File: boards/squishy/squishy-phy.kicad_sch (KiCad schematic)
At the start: 5 parts, among them Q2 Q_NMOS_GSD, U1 LFE5U-45F-8BG256

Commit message: hardware: cleaned up the schematics a bit and made them more unified
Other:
- company: (none) -> Shrine Maiden Heavy Industries
- title: (none) -> Squishy - Multitool - SCSI PHY
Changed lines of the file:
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@@
 (kicad_sch (version 20211123) (generator eeschema)
-  (paper "A4")
+  (paper "A3")
+  (title_block
+    (title "Squishy - Multitool - SCSI PHY")
+    (date "2021-12-21")
+    (rev "2")
+    (company "Shrine Maiden Heavy Industries")
+    (comment 1 "License:  CERN-OHL-S")
+    (comment 2 "© 2020 Aki 'lethalbit' Van Ness, et. al.")
+    (comment 3 "Multi-voltaga diff/se SCSI PHY for SCSI-1 2 and 3")
+    (comment 4 "Squishy - SCSI multitool and gateware library")
+  )
   (junction (at 199.39 59.69) (diameter 0) (color 0 0 0 0)
   )
@@
   (symbol (lib_id "power:GND") (at 199.39 74.93 0) (unit 1)
     (in_bom yes) (on_board yes)
-    (property "Reference" "#PWR?" (id 0) (at 199.39 81.28 0)
+    (property "Reference" "#PWR024" (id 0) (at 199.39 81.28 0)
       (effects (font (size 1.27 1.27)) hide)
     )
@@
   (symbol (lib_id "power:+3V3") (at 199.39 49.53 0) (unit 1)
     (in_bom yes) (on_board yes)
-    (property "Reference" "#PWR?" (id 0) (at 199.39 53.34 0)
+    (property "Reference" "#PWR023" (id 0) (at 199.39 53.34 0)
       (effects (font (size 1.27 1.27)) hide)
     )

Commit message: hardware: some ERC cleanup
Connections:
- no-connect marks 89 -> 88
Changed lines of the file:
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@@
   (no_connect (at 86.36 43.18))
   (no_connect (at 125.73 163.83))
-  (no_connect (at 123.19 78.74))
   (no_connect (at 121.92 55.88))
   (no_connect (at 85.09 80.01))

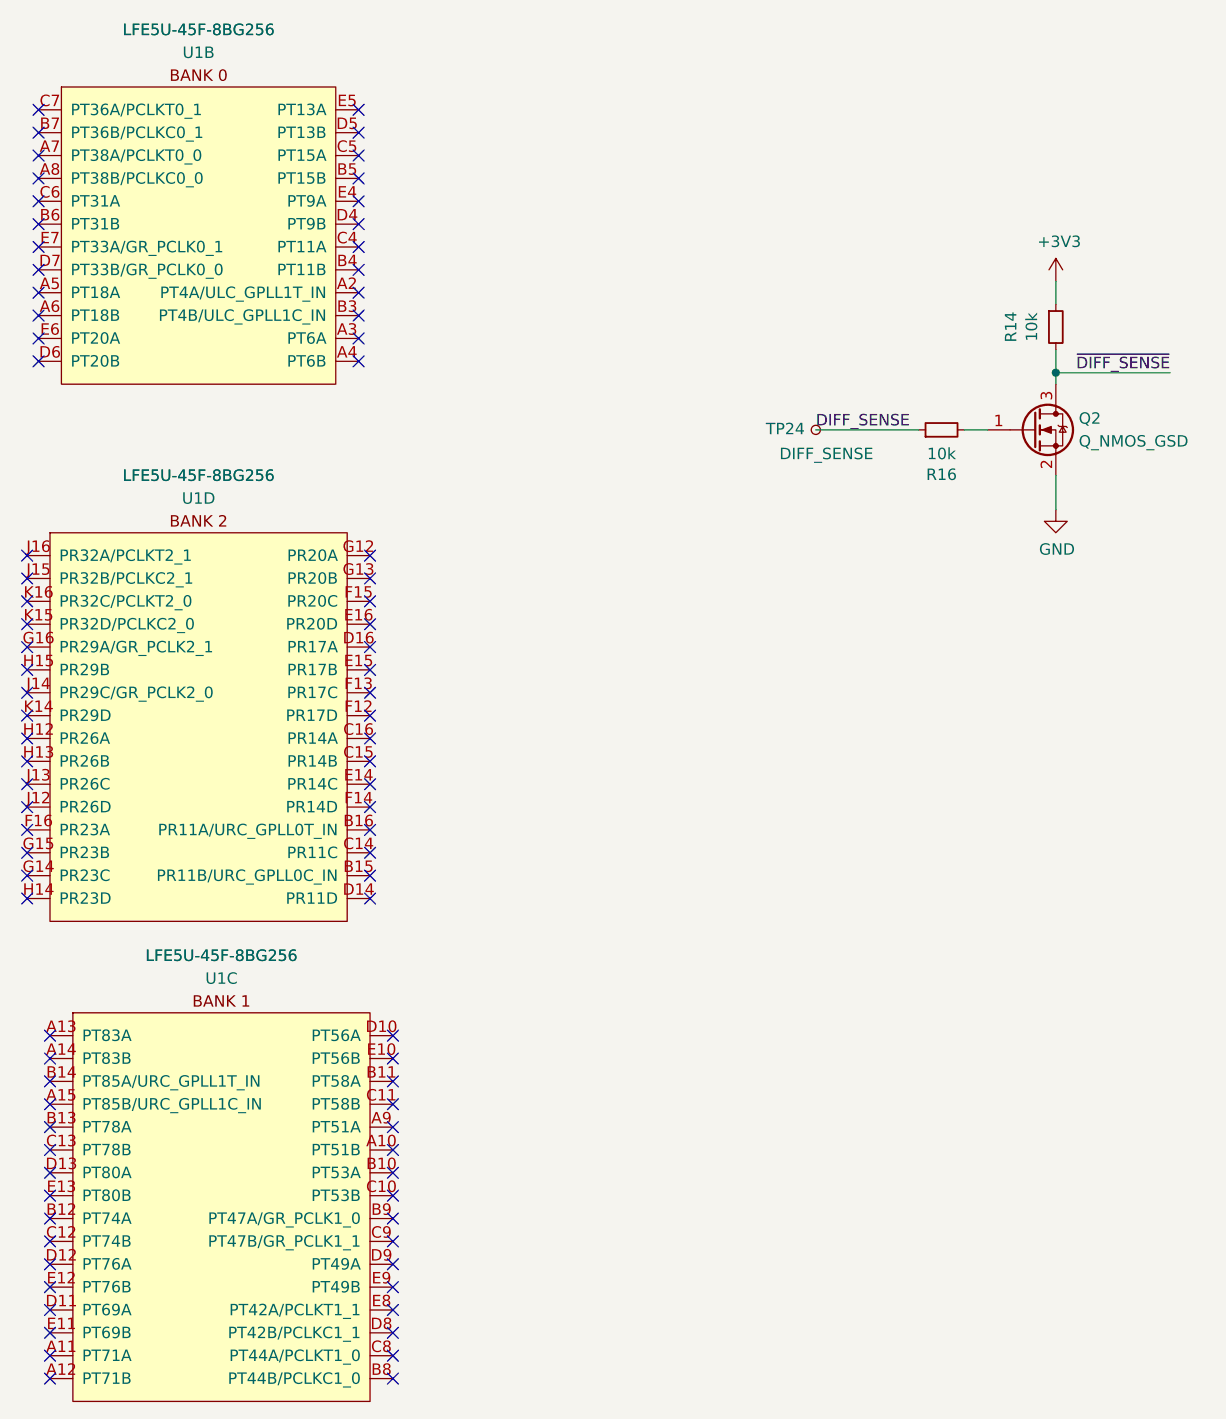
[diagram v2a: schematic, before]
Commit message: hardware: started gutting the old FPGA in preparation to migrate to the new FPGA
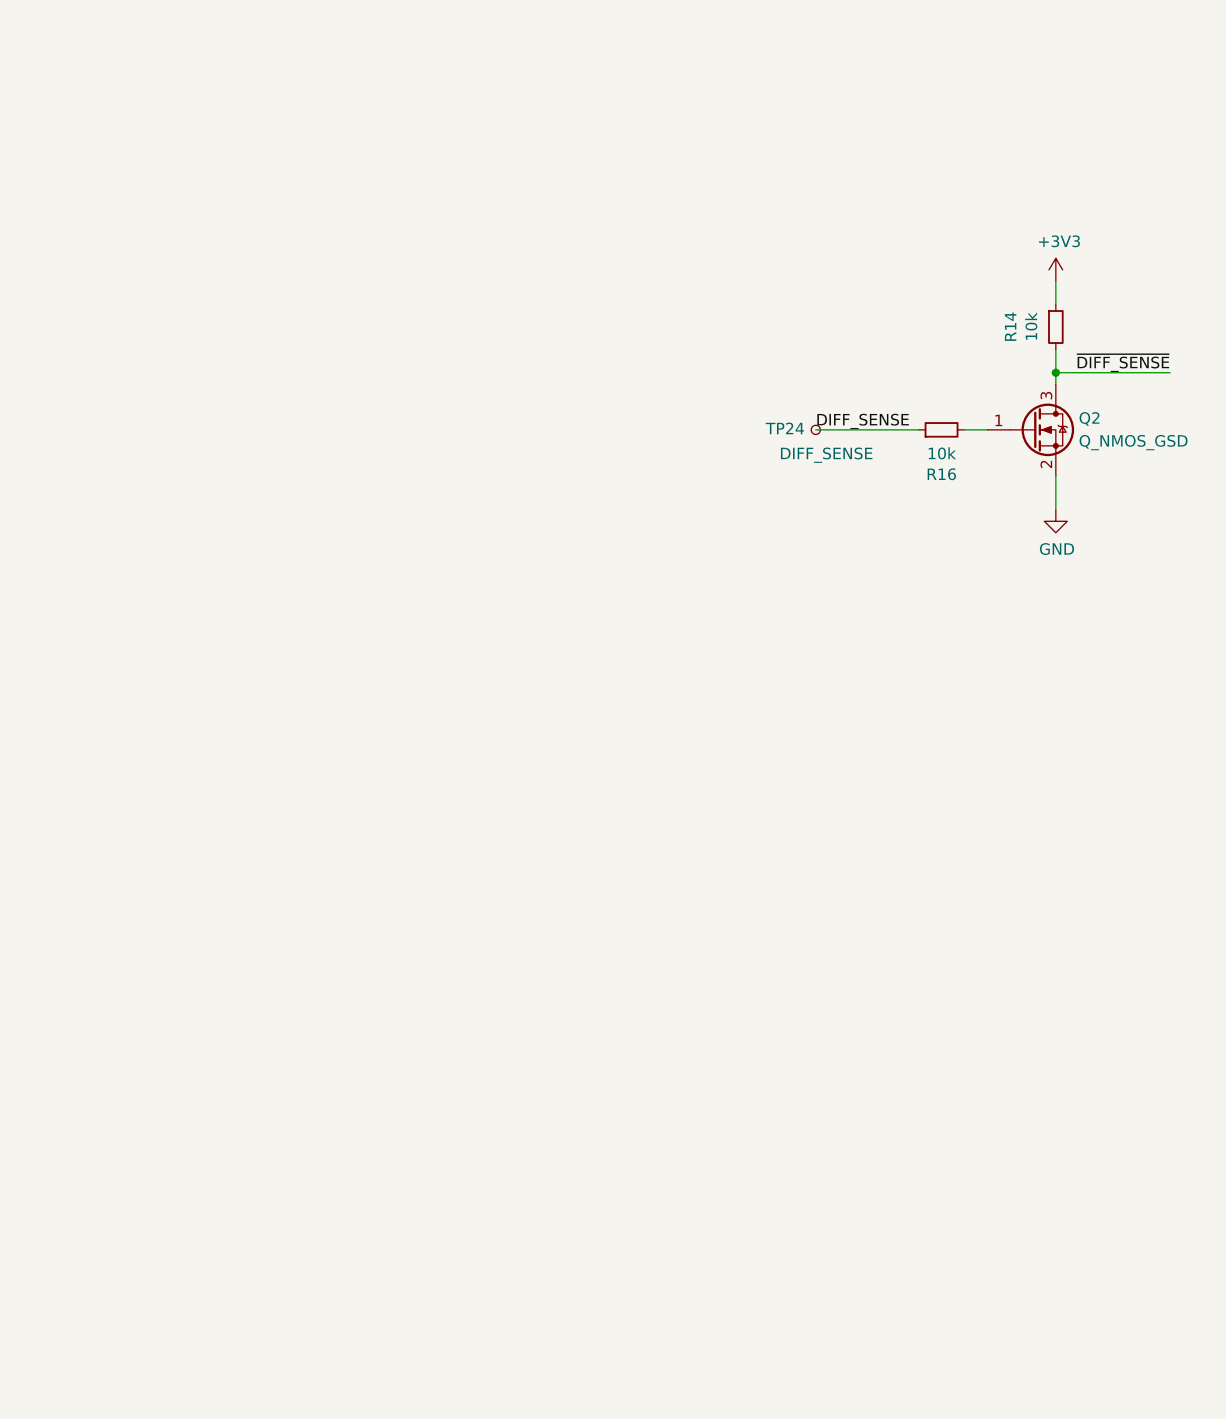
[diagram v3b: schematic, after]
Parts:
- removed U1: LFE5U-45F-8BG256, lethalbit:BGA-256_16x16_14.0x14.0mm, symbol lethalbit:LFE5U-45F-8BG381
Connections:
- no-connect marks 88 -> 0
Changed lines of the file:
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@@
   (junction (at 199.39 59.69) (diameter 0) (color 0 0 0 0)
   )
-  (no_connect (at 125.73 153.67))
-  (no_connect (at 121.92 33.02))
-  (no_connect (at 123.19 105.41))
-  (no_connect (at 87.63 151.13))
-  (no_connect (at 123.19 110.49))
-  (no_connect (at 85.09 95.25))
-  (no_connect (at 121.92 35.56))
-  (no_connect (at 125.73 151.13))
-  (no_connect (at 86.36 30.48))
-  (no_connect (at 123.19 97.79))
-  (no_connect (at 86.36 40.64))
-  (no_connect (at 123.19 118.11))
-  (no_connect (at 123.19 85.09))
-  (no_connect (at 85.09 87.63))
-  (no_connect (at 123.19 100.33))
-  (no_connect (at 85.09 85.09))
-  (no_connect (at 85.09 92.71))
-  (no_connect (at 121.92 45.72))
-  (no_connect (at 123.19 90.17))
-  (no_connect (at 125.73 158.75))
-  (no_connect (at 86.36 53.34))
-  (no_connect (at 121.92 50.8))
-  (no_connect (at 121.92 40.64))
-  (no_connect (at 85.09 115.57))
-  (no_connect (at 87.63 156.21))
-  (no_connect (at 125.73 133.35))
-  (no_connect (at 125.73 138.43))
-  (no_connect (at 87.63 166.37))
-  (no_connect (at 123.19 82.55))
-  (no_connect (at 85.09 105.41))
-  (no_connect (at 86.36 33.02))
-  (no_connect (at 85.09 100.33))
-  (no_connect (at 121.92 48.26))
-  (no_connect (at 87.63 153.67))
-  (no_connect (at 121.92 38.1))
-  (no_connect (at 87.63 143.51))
-  (no_connect (at 86.36 48.26))
-  (no_connect (at 123.19 113.03))
-  (no_connect (at 125.73 171.45))
-  (no_connect (at 121.92 43.18))
-  (no_connect (at 125.73 161.29))
-  (no_connect (at 125.73 156.21))
-  (no_connect (at 87.63 161.29))
-  (no_connect (at 87.63 140.97))
-  (no_connect (at 121.92 30.48))
-  (no_connect (at 125.73 135.89))
-  (no_connect (at 85.09 107.95))
-  (no_connect (at 86.36 43.18))
-  (no_connect (at 125.73 163.83))
-  (no_connect (at 121.92 55.88))
-  (no_connect (at 85.09 80.01))
-  (no_connect (at 123.19 87.63))
-  (no_connect (at 87.63 148.59))
-  (no_connect (at 123.19 95.25))
-  (no_connect (at 86.36 58.42))
-  (no_connect (at 125.73 146.05))
-  (no_connect (at 85.09 97.79))
-  (no_connect (at 86.36 50.8))
-  (no_connect (at 86.36 55.88))
-  (no_connect (at 123.19 102.87))
-  (no_connect (at 123.19 92.71))
-  (no_connect (at 125.73 143.51))
-  (no_connect (at 85.09 90.17))
-  (no_connect (at 125.73 168.91))
-  (no_connect (at 85.09 110.49))
-  (no_connect (at 87.63 146.05))
-  (no_connect (at 87.63 163.83))
-  (no_connect (at 87.63 168.91))
-  (no_connect (at 123.19 107.95))
-  (no_connect (at 87.63 135.89))
-  (no_connect (at 121.92 53.34))
-  (no_connect (at 125.73 166.37))
-  (no_connect (at 87.63 171.45))
-  (no_connect (at 85.09 113.03))
-  (no_connect (at 87.63 133.35))
-  (no_connect (at 87.63 138.43))
-  (no_connect (at 87.63 158.75))
-  (no_connect (at 123.19 80.01))
-  (no_connect (at 121.92 58.42))
-  (no_connect (at 123.19 115.57))
-  (no_connect (at 125.73 140.97))
-  (no_connect (at 85.09 118.11))
-  (no_connect (at 85.09 102.87))
-  (no_connect (at 86.36 38.1))
-  (no_connect (at 86.36 45.72))
-  (no_connect (at 125.73 148.59))
-  (no_connect (at 86.36 35.56))
-  (no_connect (at 85.09 82.55))
   (wire (pts (xy 199.39 49.53) (xy 199.39 52.07))
     (stroke (width 0) (type solid) (color 0 0 0 0))
@@
     (pin "1")
   )
-  (symbol (lib_id "lethalbit:LFE5U-45F-8BG381") (at 104.14 30.48 0) (unit 2)
-    (in_bom yes) (on_board yes)
-    (property "Reference" "U1" (id 0) (at 104.14 24.13 0))
-    (property "Value" "LFE5U-45F-8BG256" (id 1) (at 104.14 21.59 0))
-    (property "Footprint" "lethalbit:BGA-256_16x16_14.0x14.0mm" (id 2) (at 104.14 15.24 0)
-      (effects (font (size 1.27 1.27)) hide)
-    )
-    (property "Datasheet" "https://4donline.ihs.com/images/VipMasterIC/IC/LATT/LATT-S-A0011156806/LATT-S-A0011461202-1.pdf?hkey=CECEF36DEECDED6468708AAF2E19C0C6" (id 3) (at 104.14 12.7 0)
-      (effects (font (size 1.27 1.27)) hide)
-    )
-    (property "MFR" "Lattice" (id 4) (at 104.14 17.78 0)
-      (effects (font (size 1.27 1.27)) hide)
-    )
-    (property "MPN" "LFE5U-45F-8BG256" (id 5) (at 104.14 21.59 0))
-    (pin "A2")
-    (pin "A3")
-    (pin "A4")
-    (pin "A5")
-    (pin "A6")
-    (pin "A7")
-    (pin "A8")
-    (pin "B3")
-    (pin "B4")
-    (pin "B5")
-    (pin "B6")
-    (pin "B7")
-    (pin "C4")
-    (pin "C5")
-    (pin "C6")
-    (pin "C7")
-    (pin "D4")
-    (pin "D5")
-    (pin "D6")
-    (pin "D7")
-    (pin "E4")
-    (pin "E5")
-    (pin "E6")
-    (pin "E7")
-  )
   (symbol (lib_id "power:+3V3") (at 199.39 49.53 0) (unit 1)
     (in_bom yes) (on_board yes)
@@
     )
     (pin "1")
-  )
-  (symbol (lib_id "lethalbit:LFE5U-45F-8BG381") (at 104.14 80.01 0) (unit 4)
-    (in_bom yes) (on_board yes)
-    (property "Reference" "U1" (id 0) (at 104.14 73.66 0))
-    (property "Value" "LFE5U-45F-8BG256" (id 1) (at 104.14 71.12 0))
-    (property "Footprint" "lethalbit:BGA-256_16x16_14.0x14.0mm" (id 2) (at 104.14 64.77 0)
-      (effects (font (size 1.27 1.27)) hide)
-    )
-    (property "Datasheet" "https://4donline.ihs.com/images/VipMasterIC/IC/LATT/LATT-S-A0011156806/LATT-S-A0011461202-1.pdf?hkey=CECEF36DEECDED6468708AAF2E19C0C6" (id 3) (at 104.14 62.23 0)
-      (effects (font (size 1.27 1.27)) hide)
-    )
-    (property "MFR" "Lattice" (id 4) (at 104.14 67.31 0)
-      (effects (font (size 1.27 1.27)) hide)
-    )
-    (property "MPN" "LFE5U-45F-8BG256" (id 5) (at 104.14 71.12 0))
-    (pin "B15")
-    (pin "B16")
-    (pin "C14")
-    (pin "C15")
-    (pin "C16")
-    (pin "D14")
-    (pin "D16")
-    (pin "E14")
-    (pin "E15")
-    (pin "E16")
-    (pin "F12")
-    (pin "F13")
-    (pin "F14")
-    (pin "F15")
-    (pin "F16")
-    (pin "G12")
-    (pin "G13")
-    (pin "G14")
-    (pin "G15")
-    (pin "G16")
-    (pin "H12")
-    (pin "H13")
-    (pin "H14")
-    (pin "H15")
-    (pin "J12")
-    (pin "J13")
-    (pin "J14")
-    (pin "J15")
-    (pin "J16")
-    (pin "K14")
-    (pin "K15")
-    (pin "K16")
   )
   (symbol (lib_id "Device:R_Small") (at 186.69 66.04 90) (unit 1)
@@
     (pin "2")
   )
-  (symbol (lib_id "lethalbit:LFE5U-45F-8BG381") (at 106.68 133.35 0) (unit 3)
-    (in_bom yes) (on_board yes)
-    (property "Reference" "U1" (id 0) (at 106.68 127 0))
-    (property "Value" "LFE5U-45F-8BG256" (id 1) (at 106.68 124.46 0))
-    (property "Footprint" "lethalbit:BGA-256_16x16_14.0x14.0mm" (id 2) (at 106.68 118.11 0)
-      (effects (font (size 1.27 1.27)) hide)
-    )
-    (property "Datasheet" "https://4donline.ihs.com/images/VipMasterIC/IC/LATT/LATT-S-A0011156806/LATT-S-A0011461202-1.pdf?hkey=CECEF36DEECDED6468708AAF2E19C0C6" (id 3) (at 106.68 115.57 0)
-      (effects (font (size 1.27 1.27)) hide)
-    )
-    (property "MFR" "Lattice" (id 4) (at 106.68 120.65 0)
-      (effects (font (size 1.27 1.27)) hide)
-    )
-    (property "MPN" "LFE5U-45F-8BG256" (id 5) (at 106.68 124.46 0))
-    (pin "A10")
-    (pin "A11")
-    (pin "A12")
-    (pin "A13")
-    (pin "A14")
-    (pin "A15")
-    (pin "A9")
-    (pin "B10")
-    (pin "B11")
-    (pin "B12")
-    (pin "B13")
-    (pin "B14")
-    (pin "B8")
-    (pin "B9")
-    (pin "C10")
-    (pin "C11")
-    (pin "C12")
-    (pin "C13")
-    (pin "C8")
-    (pin "C9")
-    (pin "D10")
-    (pin "D11")
-    (pin "D12")
-    (pin "D13")
-    (pin "D8")
-    (pin "D9")
-    (pin "E10")
-    (pin "E11")
-    (pin "E12")
-    (pin "E13")
-    (pin "E8")
-    (pin "E9")
-  )
 )
